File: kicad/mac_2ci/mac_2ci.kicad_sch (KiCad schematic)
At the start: 16 parts, among them U2 74HC00, U3 74HC00

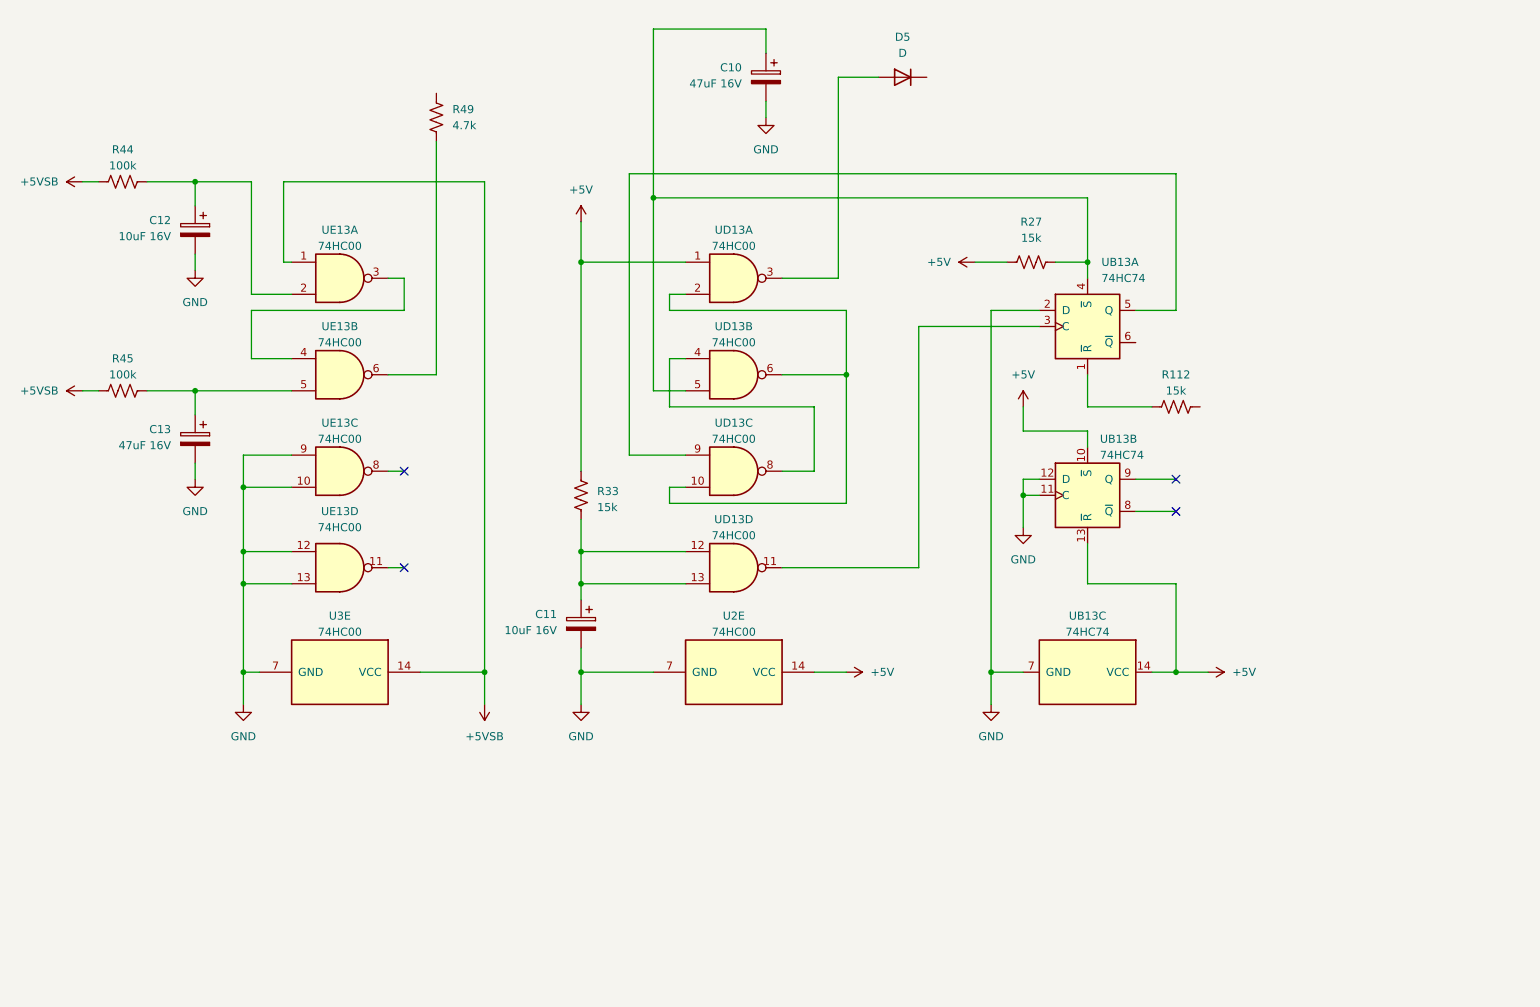
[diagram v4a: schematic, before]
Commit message: Update mac_2ci schematic
- Add rear power button
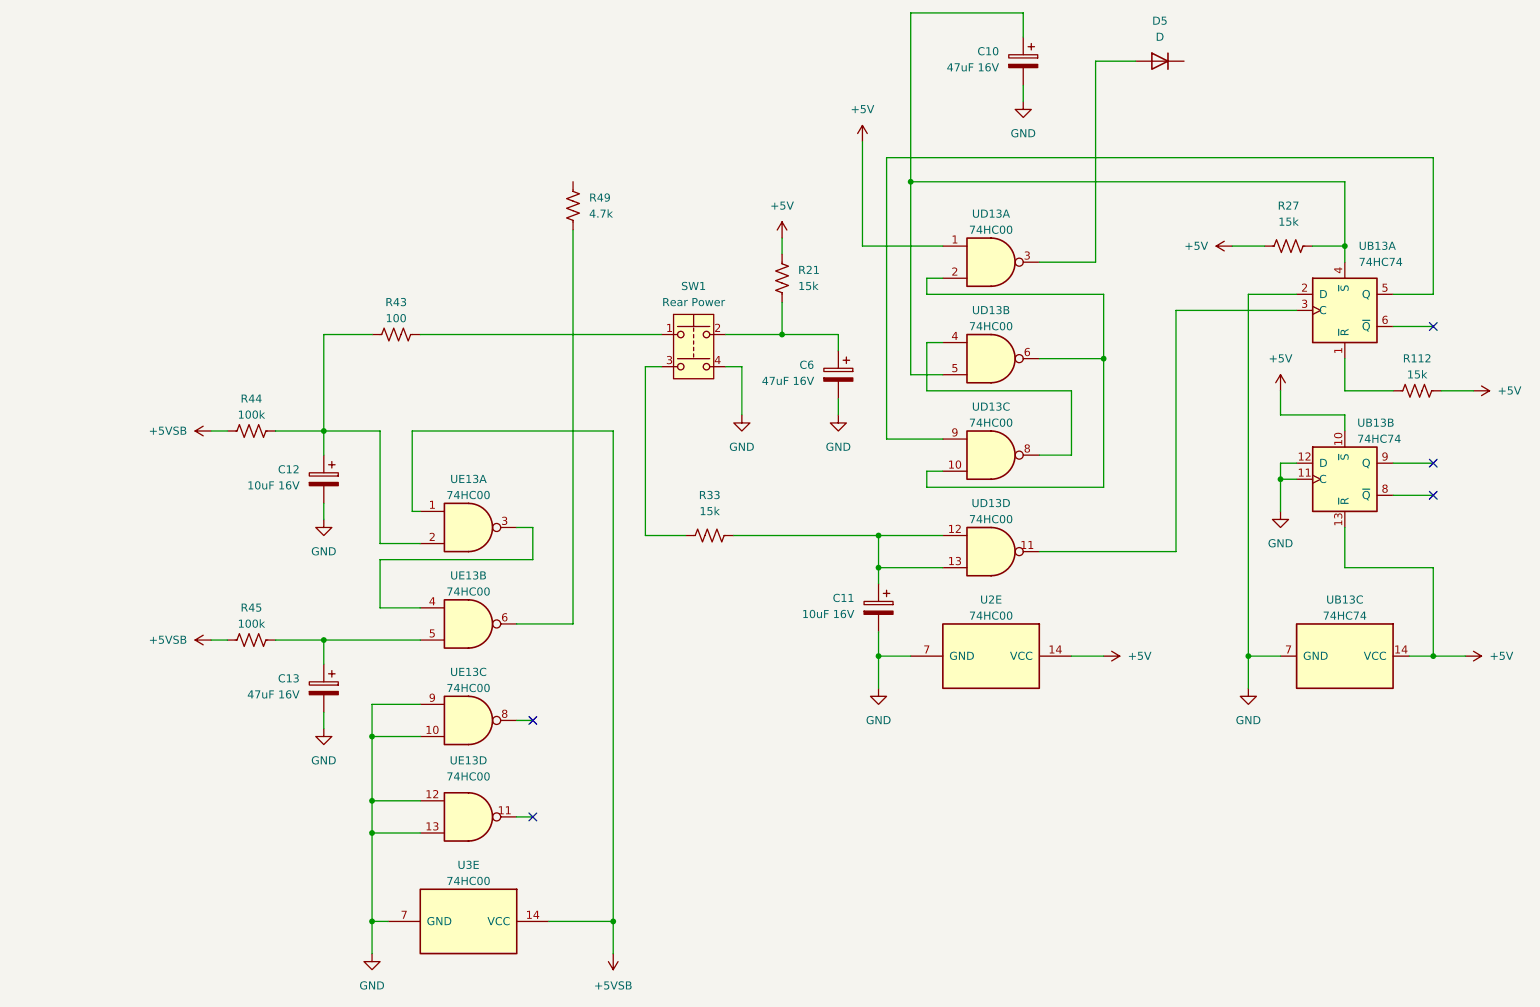
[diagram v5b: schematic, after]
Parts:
- added C6: 47uF 16V, symbol Device:C_Polarized
- added R21: 15k, symbol Device:R_US
- added R43: 100, symbol Device:R_US
- added SW1: Rear Power, symbol Switch:SW_Push_Dual
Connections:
- net +5V: now also R112.2, R21.1; no longer R33.1
- net GND: now also C6.2, SW1.4
- net at C12.1, R44.2, UE13.2: now also R43.1
- new net: R43.2, SW1.1
- new net: C6.1, R21.2, SW1.2
- new net: R33.1, SW1.3
- no-connect marks 4 -> 5
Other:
- moved on the sheet: C10, C11, C12, C13, D5, R112, R27, R33, R44, R45, R49, U2E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
